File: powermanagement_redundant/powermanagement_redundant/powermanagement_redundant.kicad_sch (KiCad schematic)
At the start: 41 parts, among them J1 Screw_Terminal_01x01, J2 Screw_Terminal_01x01, J3 Screw_Terminal_01x01, J4 Screw_Terminal_01x01, J5 Screw_Terminal_01x01, J6 Screw_Terminal_01x01, J7 Screw_Terminal_01x01, J8 Screw_Terminal_01x01, J9 691323300002, SW1 SW_DIP_x01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

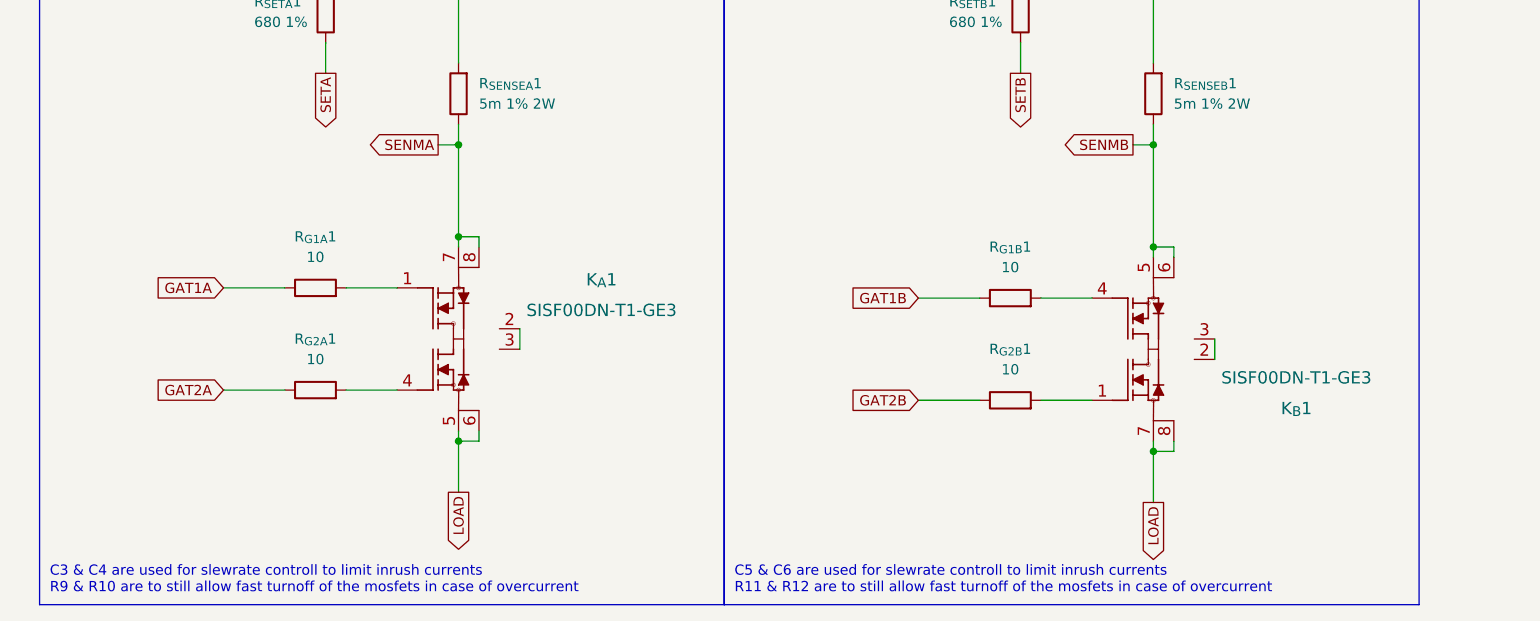
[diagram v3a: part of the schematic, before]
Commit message: Mosfets getauscht.
Die Mosfets hab ich gegen CSD87313DMS getauscht. Im gleichen Schritt hab ich die Pads überarbeitet. Die haben jetzt einen vollständigen Übergangauf zum Backlayer.
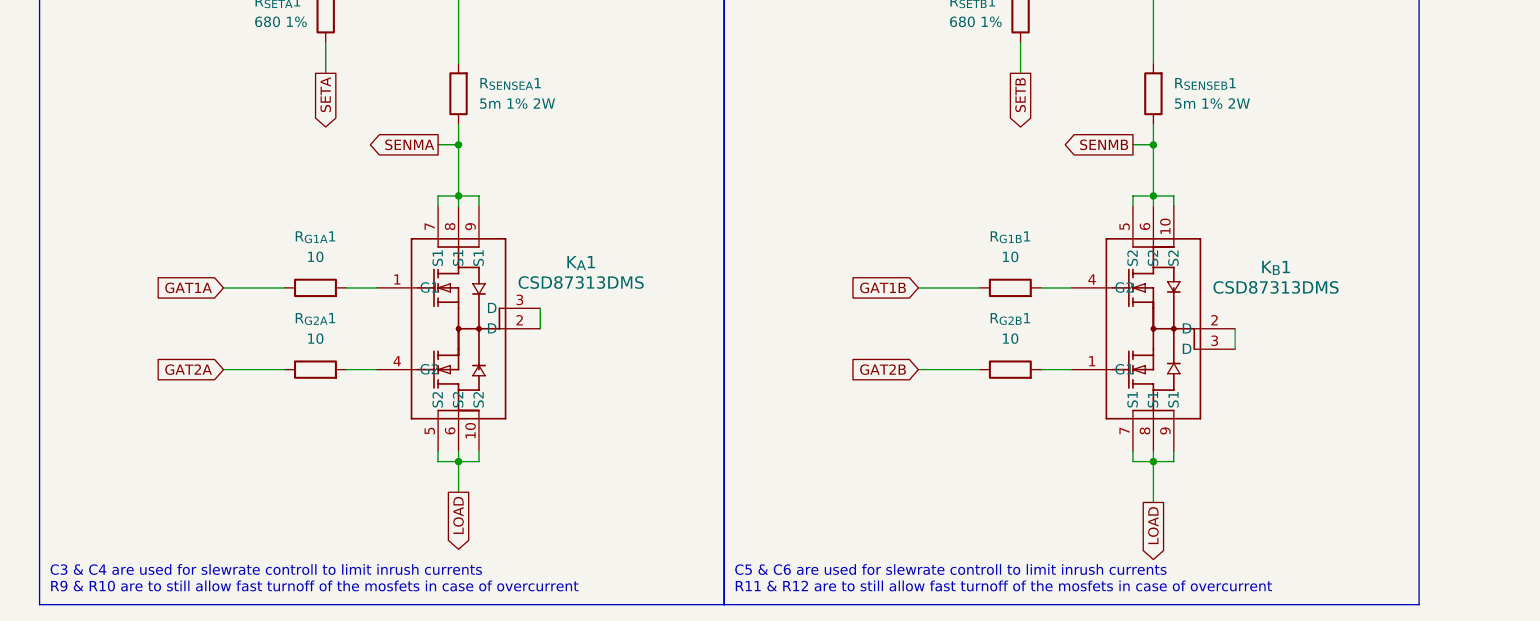
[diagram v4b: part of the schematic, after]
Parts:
- removed K_{A}1, K_{B}1: SISF00DN-T1-GE3, SISF00DN-1:SISF00DN-T1-GE3, symbol SISF00DN-T1:SISF00DN-T1-GE3
- added K_{A}1: CSD87313DMS, CSD87313DMS:DMS0008A, symbol 20CSD87313DMS:CSD87313DMS
- added K_{B}1: CSD87313DMS, DMS0008A, symbol 20CSD87313DMS:CSD87313DMS
- J1, J2, J3, J4, J5, J6, J7, J8: footprint MountingHole:MountingHole_3.2mm_M3_Pad_Via -> MountingHole:MountingHole_3.5mm_Pad
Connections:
- net LOAD: now also K_{A}1.10 (S2), K_{A}1.5 (S2), K_{A}1.6 (S2), K_{B}1.7 (S1), K_{B}1.8 (S1), K_{B}1.9 (S1)
- net SENMA: now also K_{A}1.7 (S1), K_{A}1.8 (S1), K_{A}1.9 (S1)
- net SENMB: now also K_{B}1.10 (S2), K_{B}1.5 (S2), K_{B}1.6 (S2)
- net at R_{G1B}1.2: now also K_{B}1.4 (G2)
- net at R_{G1A}1.2: now also K_{A}1.1 (G1)
- net at R_{G2A}1.2: now also K_{A}1.4 (G2)
- net at R_{G2B}1.2: now also K_{B}1.1 (G1)
- new net: K_{A}1.2 (D), K_{A}1.3 (D)
- new net: K_{B}1.2 (D), K_{B}1.3 (D)
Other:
- moved on the sheet: R_{G1B}1, R_{G2A}1, R_{G2B}1

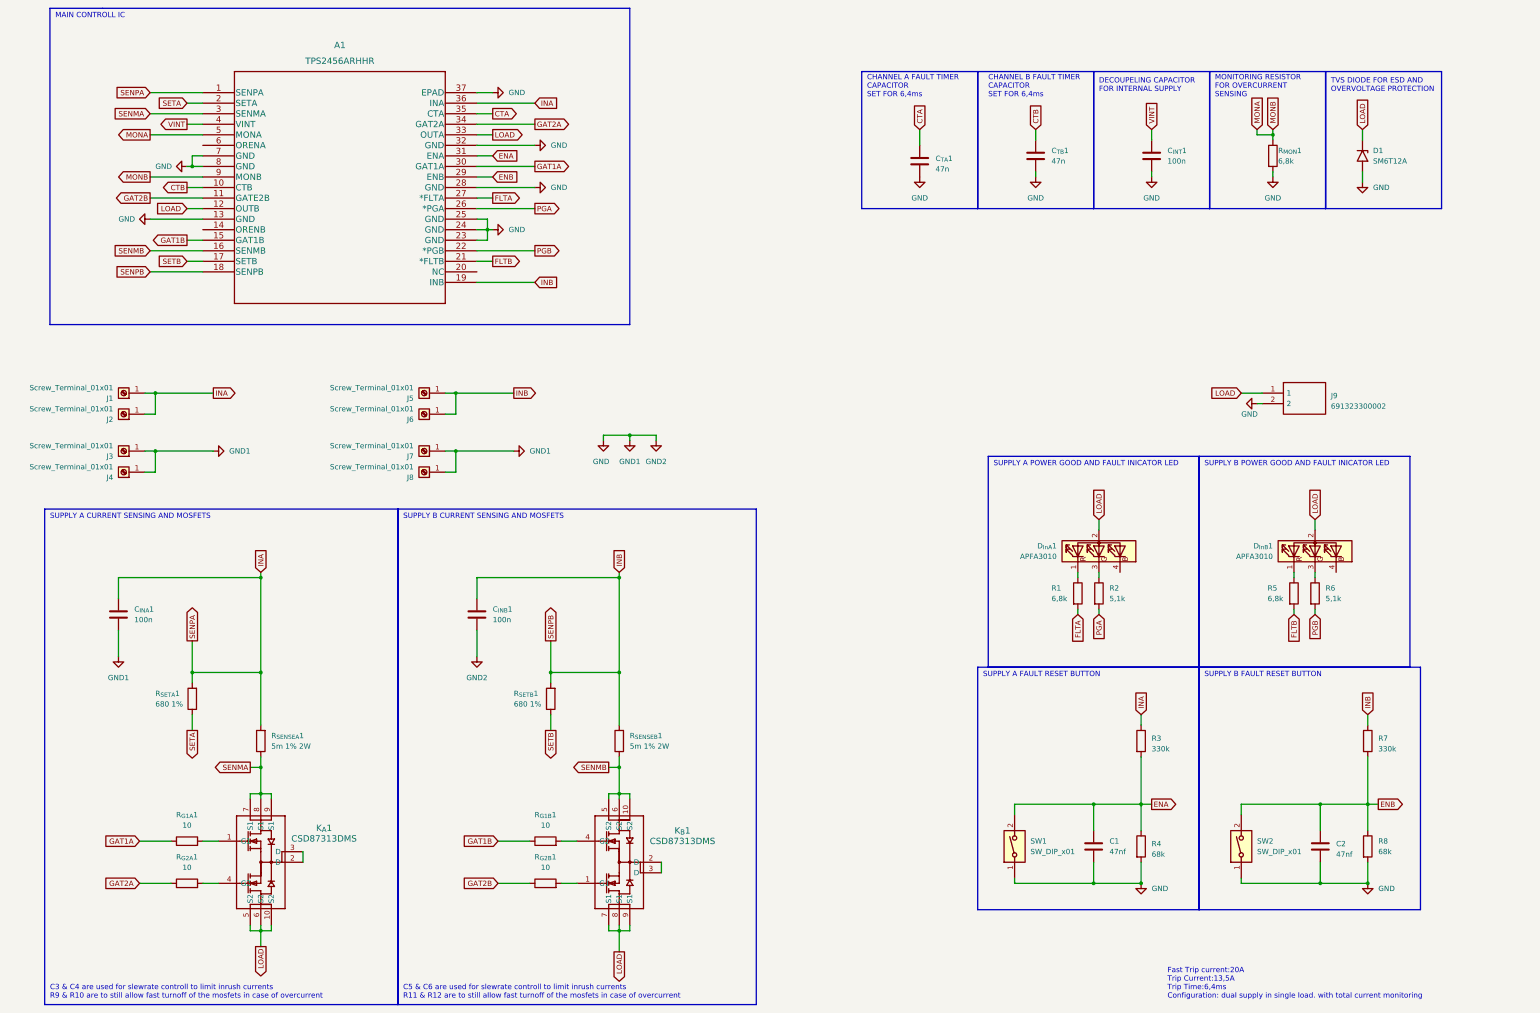
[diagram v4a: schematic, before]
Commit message: Kompletto auf anderes ic umgebaut
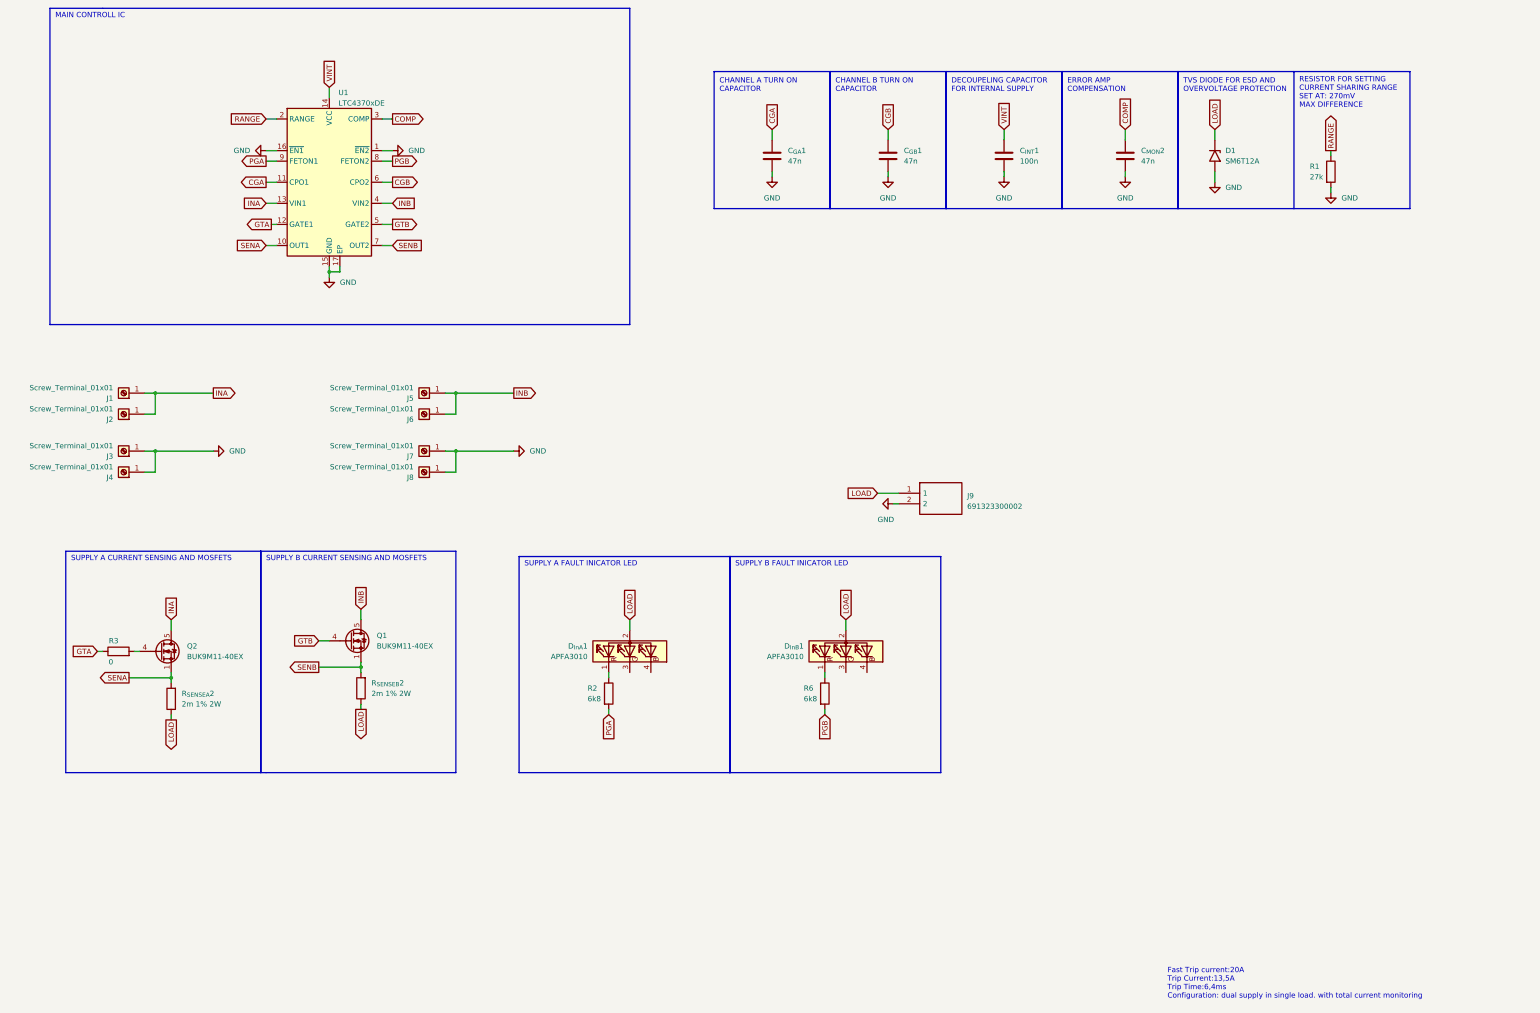
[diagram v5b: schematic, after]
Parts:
- removed A1: TPS2456ARHHR, TPS2456:TPS2456ARHHR, symbol TPS2456:TPS2456ARHHR
- removed C1, C2: 47nf, Capacitor_SMD:C_0805_2012Metric, symbol Device:C
- removed C_{INA}1, C_{INB}1: 100n, Capacitor_SMD:C_0805_2012Metric, symbol Device:C
- removed K_{A}1: CSD87313DMS, CSD87313DMS:DMS0008A, symbol 20CSD87313DMS:CSD87313DMS
- removed K_{B}1: CSD87313DMS, DMS0008A, symbol 20CSD87313DMS:CSD87313DMS
- removed R4, R8: 68k, Resistor_SMD:R_0805_2012Metric, symbol Device:R
- removed R5, R_{MON}1: 6,8k, Resistor_SMD:R_0805_2012Metric, symbol Device:R
- removed R7: 330k, Resistor_SMD:R_0805_2012Metric, symbol Device:R
- removed R_{G1A}1, R_{G1B}1, R_{G2A}1, R_{G2B}1: 10, Resistor_SMD:R_0805_2012Metric, symbol Device:R
- removed R_{SENSEA}1, R_{SENSEB}1: 5m 1% 2W, Resistor_SMD:R_0612_1632Metric, symbol Device:R
- removed R_{SETA}1, R_{SETB}1: 680 1%, Resistor_SMD:R_0805_2012Metric, symbol Device:R
- removed SW1, SW2: SW_DIP_x01, Button_Switch_SMD:Panasonic_EVQPUK_EVQPUB, symbol Switch:SW_DIP_x01
- added C_{MON}2: 47n, Capacitor_SMD:C_0805_2012Metric, symbol Device:C
- added Q1, Q2: BUK9M11-40EX, Package_TO_SOT_SMD:LFPAK33, symbol Transistor_FET:BUK9M11-40EX
- added R_{SENSEA}2, R_{SENSEB}2: 2m 1% 2W, Resistor_SMD:R_0612_1632Metric, symbol Device:R
- added U1: LTC4370xDE, Package_DFN_QFN:DFN-16-1EP_3x4mm_P0.45mm_EP1.7x3.3mm, symbol Power_Management:LTC4370xDE
- R1: value 6,8k -> 27k
- R2, R6: value 5,1k -> 6k8
- R3: value 330k -> 0
- renumbered C_{TA}1 to C_{GA}1, C_{TB}1 to C_{GB}1
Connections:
- net FLTA is gone; now on net GND: R1.2
- net GND: now also C_{MON}2.2, U1.1 (~{EN2}), U1.15 (GND), U1.16 (~{EN1}), U1.17 (EP)
- net INA: now also Q2.5 (D), U1.13 (VIN1); no longer R3.1
- net INB: now also Q1.5 (D), U1.4 (VIN2)
- net LOAD: now also R_{SENSEA}2.1, R_{SENSEB}2.1
- net PGA: now also U1.9 (FETON1)
- net PGB: now also U1.8 (FETON2)
- net VINT: now also U1.14 (VCC)
- net at D_{InB}1.1 (R): now also R6.1
- net at D_{InB}1.3 (G): no longer R6.1
- net at D_{InA}1.1 (R): now also R2.1; no longer R1.1
- net at D_{InA}1.3 (G): no longer R2.1
- net CTA renamed CGA
- net CGA: now also U1.11 (CPO1)
- net CTB renamed CGB
- net CGB: now also U1.6 (CPO2)
- net ENA: no longer names the net of R3.2
- net ENA: now also Q2.4 (G)
- new net COMP: C_{MON}2.1, U1.3 (COMP)
- new net GTA: R3.1, U1.12 (GATE1)
- new net GTB: Q1.4 (G), U1.5 (GATE2)
- new net RANGE: R1.1, U1.2 (RANGE)
- new net SENA: Q2.1 (S), Q2.2 (S), Q2.3 (S), R_{SENSEA}2.2, U1.10 (OUT1)
- new net SENB: Q1.1 (S), Q1.2 (S), Q1.3 (S), R_{SENSEB}2.2, U1.7 (OUT2)
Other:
- note added: "CHANNEL A TURN ON CAPACITOR"
- note added: "CHANNEL B TURN ON CAPACITOR"
- note added: "ERROR AMP COMPENSATION"
- note added: "RESISTOR FOR SETTING CURRENT SHARING RANGE SET AT: 270mV MAX DIFFERENCE"
- note added: "SUPPLY A FAULT INICATOR LED"
- note added: "SUPPLY B FAULT INICATOR LED"
- note removed: "C3 & C4 are used for slewrate controll to limit inrush currents R9 & R10 are to still allow fast turnoff of the mosfets in case of overcurrent"
- note removed: "C5 & C6 are used for slewrate controll to limit inrush currents R11 & R12 are to still allow fast turnoff of the mosfets in case of overcurrent"
- note removed: "CHANNEL A FAULT TIMER CAPACITOR SET FOR 6,4ms"
- note removed: "CHANNEL B FAULT TIMER CAPACITOR SET FOR 6,4ms"
- note removed: "MONITORING RESISTOR FOR OVERCURRENT SENSING"
- note removed: "SUPPLY A FAULT RESET BUTTON"
- note removed: "SUPPLY A POWER GOOD AND FAULT INICATOR LED"
- note removed: "SUPPLY B FAULT RESET BUTTON"
- note removed: "SUPPLY B POWER GOOD AND FAULT INICATOR LED"
- moved on the sheet: C_{GA}1, C_{GB}1, C_{INT}1, D1, D_{InA}1, D_{InB}1, J9, R2, R6

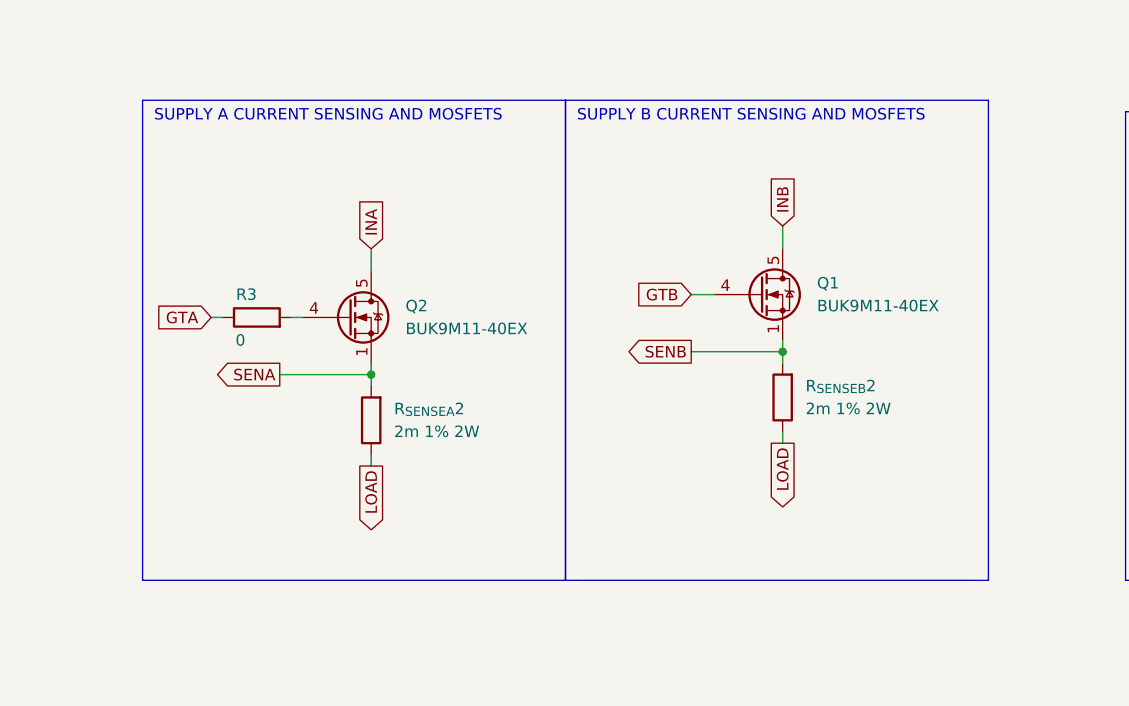
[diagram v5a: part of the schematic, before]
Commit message: N-Channel MOSFET falsche Orientierung
Die Orientierung des N-MOSFET ist geändert. Vor der Fertigung muss noch auf der PCB die Versions Nummer geändert werden.
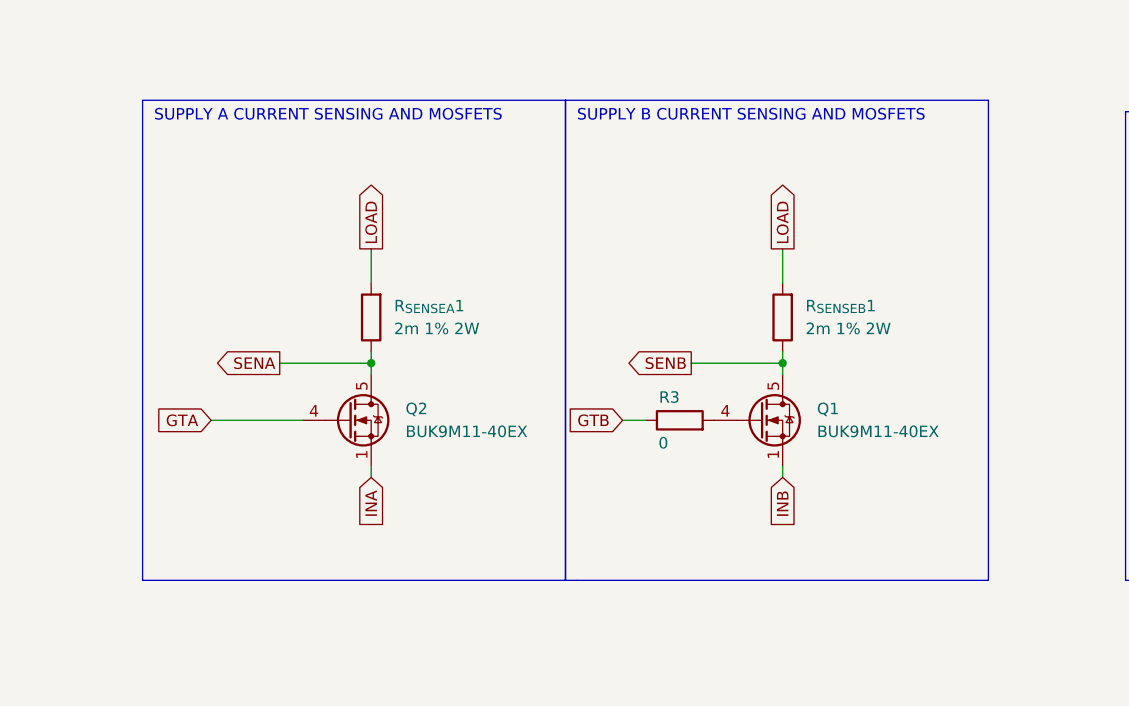
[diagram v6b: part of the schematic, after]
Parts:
- removed R_{SENSEA}2, R_{SENSEB}2: 2m 1% 2W, Resistor_SMD:R_0612_1632Metric, symbol Device:R
- added R_{SENSEA}1, R_{SENSEB}1: 2m 1% 2W, Resistor_SMD:R_0612_1632Metric, symbol Device:R
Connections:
- net GTA: now also Q2.4 (G); no longer R3.1
- net GTB: now also R3.1; no longer Q1.4 (G)
- net INA: now also Q2.1 (S), Q2.2 (S), Q2.3 (S); no longer Q2.5 (D)
- net INB: now also Q1.1 (S), Q1.2 (S), Q1.3 (S); no longer Q1.5 (D)
- net LOAD: now also R_{SENSEA}1.2, R_{SENSEB}1.2
- net SENA: now also Q2.5 (D), R_{SENSEA}1.1; no longer Q2.1 (S), Q2.2 (S), Q2.3 (S)
- net SENB: now also Q1.5 (D), R_{SENSEB}1.1; no longer Q1.1 (S), Q1.2 (S), Q1.3 (S)
- net at R3.2: now also Q1.4 (G); no longer Q2.4 (G)

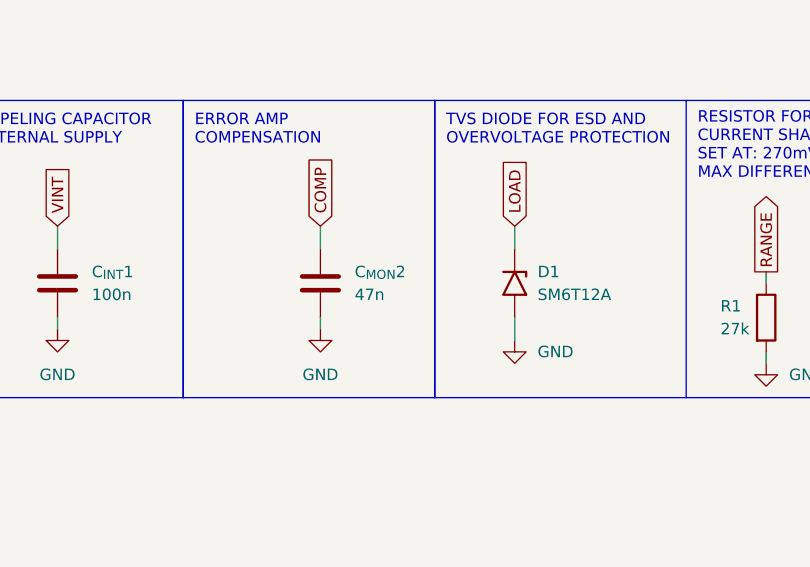
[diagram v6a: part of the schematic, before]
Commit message: Bom Erstellt
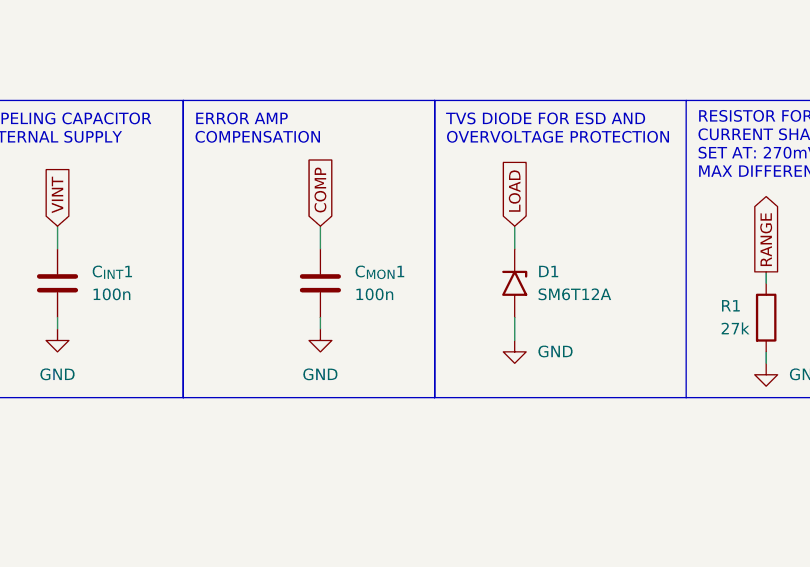
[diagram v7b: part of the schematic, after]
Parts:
- C_{MON}1: renamed from C_{MON}2; value 47n -> 100n
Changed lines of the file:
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@@
 		(dnp no)
 		(fields_autoplaced yes)
-		(property "Reference" "C_{MON}2"
+		(property "Reference" "C_{MON}1"
 			(at 294.64 58.4199 0)
 			(effects
@@
 			)
 		)
-		(property "Value" "47n"
+		(property "Value" "100n"
 			(at 294.64 60.9599 0)
 			(effects
@@
 			(project "powermanagement_redundant"
 				(path "/8a7a656b-558d-4577-8c43-8c0fcd36144c"
-					(reference "C_{MON}2")
+					(reference "C_{MON}1")
 					(unit 1)
 				)
